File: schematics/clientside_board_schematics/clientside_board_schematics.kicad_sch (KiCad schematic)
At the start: 21 parts, among them J1 12V Power Input, J10 Keylock Switch Connector, J2 UART Connector, J4 Comm Status LED, J5 12V Output, J6 Fire Button Connector, J7 5V Output, J8 LCD Connector, J9 Potentiometer Connector, T1 VXO7805-1000

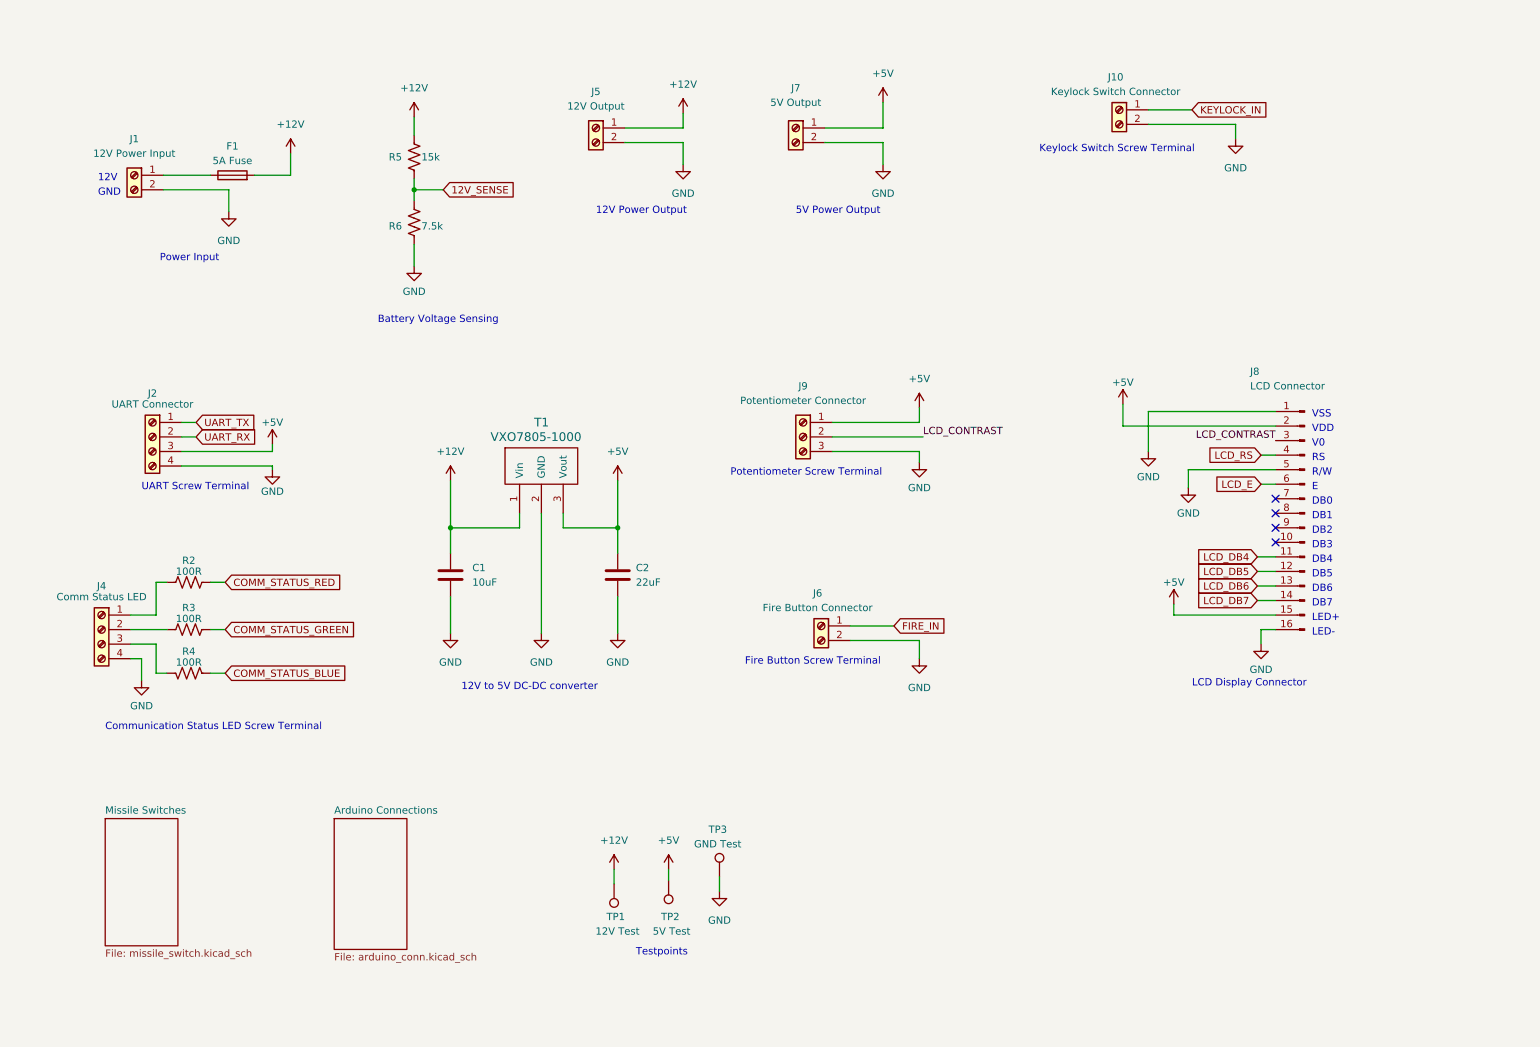
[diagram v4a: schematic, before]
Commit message: Update client-side board schematic
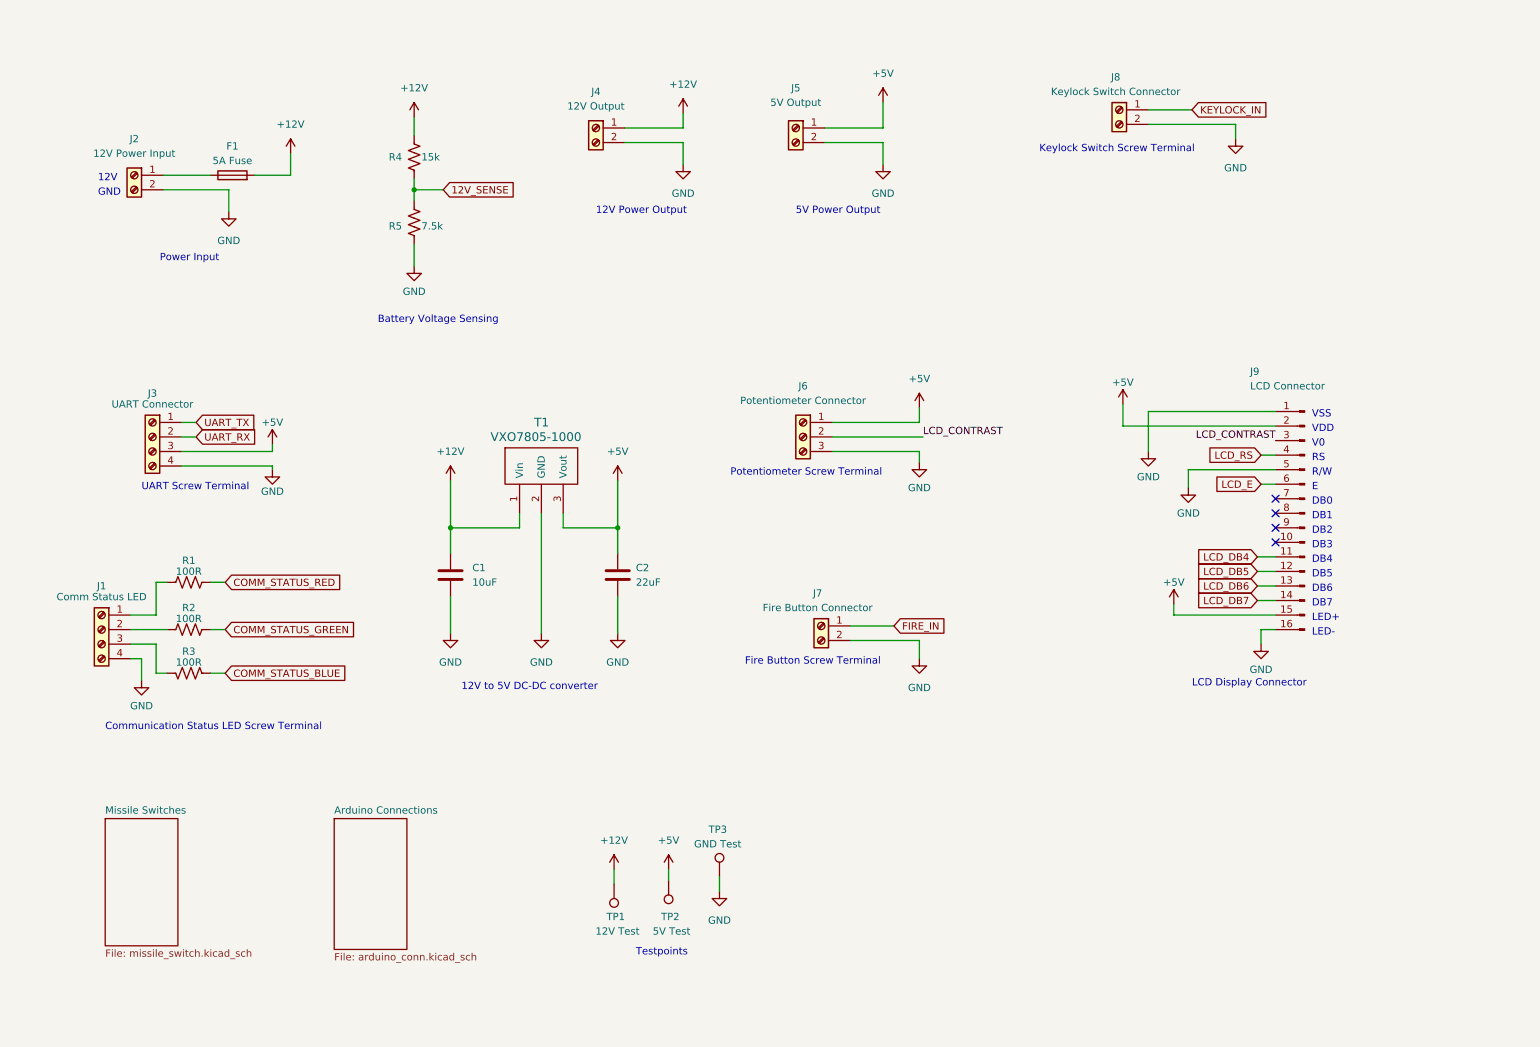
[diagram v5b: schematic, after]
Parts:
- renumbered J4 to J1, J1 to J2, J2 to J3, J5 to J4, J7 to J5, J9 to J6, J6 to J7, J10 to J8, J8 to J9, R2 to R1, R3 to R2, R4 to R3, R5 to R4, R6 to R5

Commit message: Update Client-side board schematic for reduce routing complexity
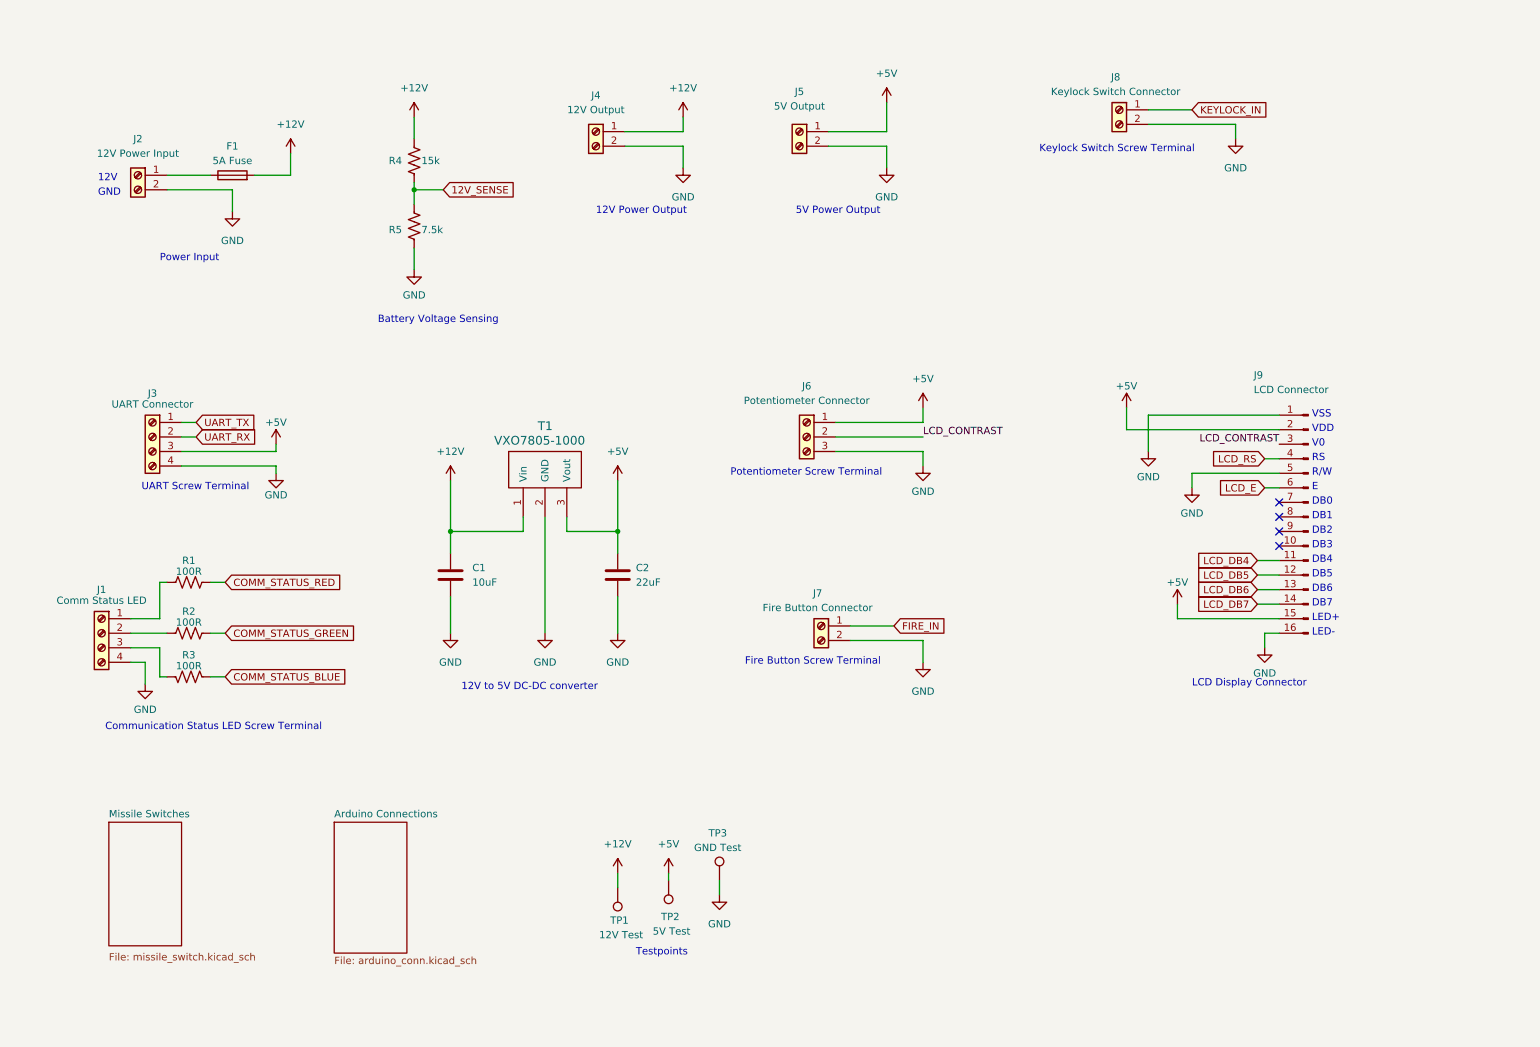
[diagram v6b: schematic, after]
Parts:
- C1, C2: footprint Capacitor_SMD:C_0805_2012Metric_Pad1.15x1.40mm_HandSolder -> Capacitor_SMD:C_0805_2012Metric_Pad1.18x1.45mm_HandSolder
- J3: footprint (none) -> TerminalBlock_Phoenix:TerminalBlock_Phoenix_PT-1,5-4-3.5-H_1x04_P3.50mm_Horizontal
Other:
- moved on the sheet: J1, J2, J4, J5, J6, J9, R2, R3, R4, R5, T1, TP1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

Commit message: Update Client-side board layout
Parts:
- J9: footprint Connector_PinSocket_2.54mm:PinSocket_1x16_P2.54mm_Vertical -> clientside_footprints:NHD-0420DZ-FSW-FBW
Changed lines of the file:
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@@
       (effects (font (size 1.27 1.27)) (justify right))
     )
-    (property "Footprint" "Connector_PinSocket_2.54mm:PinSocket_1x16_P2.54mm_Vertical" (at 242.57 102.87 0)
+    (property "Footprint" "clientside_footprints:NHD-0420DZ-FSW-FBW" (at 242.57 102.87 0)
       (effects (font (size 1.27 1.27)) hide)
     )

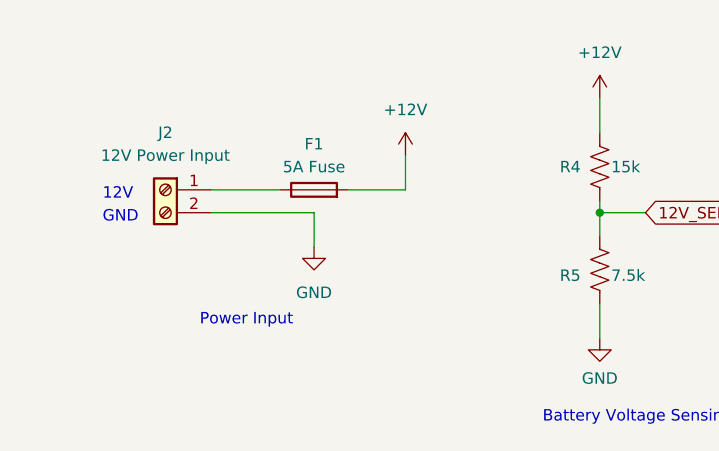
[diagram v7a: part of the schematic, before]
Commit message: Update clientside board layout
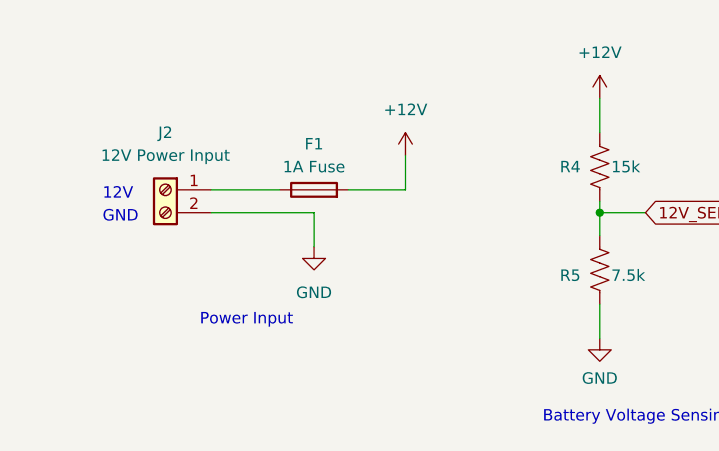
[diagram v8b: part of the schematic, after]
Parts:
- F1: value 5A Fuse -> 1A Fuse
- J1, J3: footprint TerminalBlock_Phoenix:TerminalBlock_Phoenix_PT-1,5-4-3.5-H_1x04_P3.50mm_Horizontal -> TerminalBlock_Phoenix:TerminalBlock_Phoenix_MKDS-1,5-4-5.08_1x04_P5.08mm_Horizontal
- J6: footprint TerminalBlock_Phoenix:TerminalBlock_Phoenix_PT-1,5-3-3.5-H_1x03_P3.50mm_Horizontal -> TerminalBlock_Phoenix:TerminalBlock_Phoenix_MKDS-1,5-3-5.08_1x03_P5.08mm_Horizontal
- J7, J8: footprint TerminalBlock_Phoenix:TerminalBlock_Phoenix_PT-1,5-2-3.5-H_1x02_P3.50mm_Horizontal -> TerminalBlock_Phoenix:TerminalBlock_Phoenix_MKDS-1,5-2-5.08_1x02_P5.08mm_Horizontal
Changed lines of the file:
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@@
       (effects (font (size 1.27 1.27)))
     )
-    (property "Footprint" "TerminalBlock_Phoenix:TerminalBlock_Phoenix_PT-1,5-4-3.5-H_1x04_P3.50mm_Horizontal" (at 40.64 88.9 0)
+    (property "Footprint" "TerminalBlock_Phoenix:TerminalBlock_Phoenix_MKDS-1,5-4-5.08_1x04_P5.08mm_Horizontal" (at 40.64 88.9 0)
       (effects (font (size 1.27 1.27)) hide)
     )
@@
       (effects (font (size 1.27 1.27)))
     )
-    (property "Footprint" "TerminalBlock_Phoenix:TerminalBlock_Phoenix_PT-1,5-3-3.5-H_1x03_P3.50mm_Horizontal" (at 154.94 88.9 0)
+    (property "Footprint" "TerminalBlock_Phoenix:TerminalBlock_Phoenix_MKDS-1,5-3-5.08_1x03_P5.08mm_Horizontal" (at 154.94 88.9 0)
       (effects (font (size 1.27 1.27)) hide)
     )
@@
       (effects (font (size 1.27 1.27)))
     )
-    (property "Footprint" "TerminalBlock_Phoenix:TerminalBlock_Phoenix_PT-1,5-4-3.5-H_1x04_P3.50mm_Horizontal" (at 31.75 123.19 0)
+    (property "Footprint" "TerminalBlock_Phoenix:TerminalBlock_Phoenix_MKDS-1,5-4-5.08_1x04_P5.08mm_Horizontal" (at 31.75 123.19 0)
       (effects (font (size 1.27 1.27)) hide)
     )
@@
       (effects (font (size 1.27 1.27)))
     )
-    (property "Footprint" "TerminalBlock_Phoenix:TerminalBlock_Phoenix_PT-1,5-2-3.5-H_1x02_P3.50mm_Horizontal" (at 209.55 31.75 0)
+    (property "Footprint" "TerminalBlock_Phoenix:TerminalBlock_Phoenix_MKDS-1,5-2-5.08_1x02_P5.08mm_Horizontal" (at 209.55 31.75 0)
       (effects (font (size 1.27 1.27)) hide)
     )
@@
       (effects (font (size 1.27 1.27)))
     )
-    (property "Footprint" "TerminalBlock_Phoenix:TerminalBlock_Phoenix_PT-1,5-2-3.5-H_1x02_P3.50mm_Horizontal" (at 157.48 121.92 0)
+    (property "Footprint" "TerminalBlock_Phoenix:TerminalBlock_Phoenix_MKDS-1,5-2-5.08_1x02_P5.08mm_Horizontal" (at 157.48 121.92 0)
       (effects (font (size 1.27 1.27)) hide)
     )
@@
       (effects (font (size 1.27 1.27)))
     )
-    (property "Value" "5A Fuse" (at 54.61 40.64 90)
-      (effects (font (size 1.27 1.27)))
-    )
+    (property "Value" "1A Fuse" (at 54.61 40.64 90)
+      (effects (font (size 1.27 1.27)))
+    )
